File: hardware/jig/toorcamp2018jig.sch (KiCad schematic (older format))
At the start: 76 parts, among them J1 NEIGHBOR1, J2 NEIGHBOR2, J3 GOODFET, J4 TOP_INTERCONNECT, J5 BACK_INTERCONNECT, J6 FAULT, J7 BONUS_ROW, J8 TEST_2P, J9 TEST_2P, P1 CONN_01X02, P10 CONN_01X02, P11 CONN_01X02, P12 CONN_01X02, P13 CONN_01X02, P14 CONN_01X02, P2 CONN_01X02, P3 CONN_01X02, P4 CONN_01X02, P5 CONN_01X02, P6 CONN_01X02, P7 CONN_01X02, P8 CONN_01X02, P9 CONN_01X02, U1 NX5P2553GV

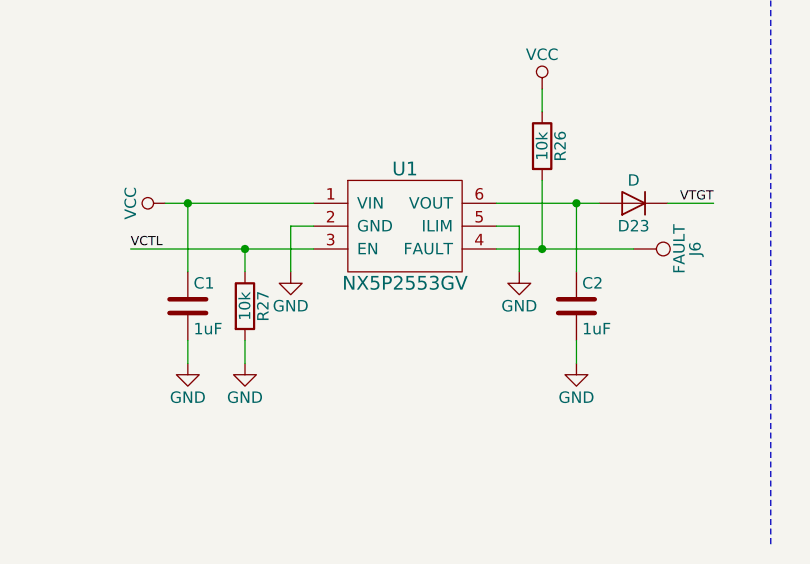
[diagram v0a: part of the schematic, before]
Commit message: filled in test jig bom info
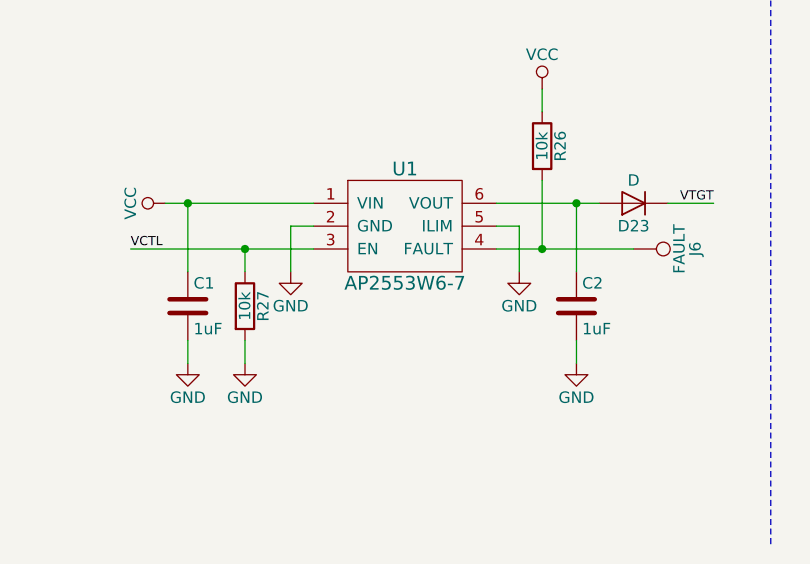
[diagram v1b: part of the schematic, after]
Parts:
- J1, J2: Description (none) -> CONN HEADER .100\" DUAL STR 40POS; Manufacturer (none) -> Sullins; Part Number (none) -> PRPC020DAAN-RC
- J4: Description (none) -> CONN RCPT .100\" 40POS DUAL-ROW GOLD; Manufacturer (none) -> Samtec; Part Number (none) -> SSW-120-01-F-D
- J5: Description (none) -> CONN HEADER .100\" DUAL R/A 40POS; Manufacturer (none) -> Sullins; Part Number (none) -> PRPC020DBAN-M71RC
- P1, P10, P11, P12, P13, P14, P2, P3, P4, P5, P6, P7, P8, P9: Description (none) -> CONN BATTERY 2 POS MINI; Manufacturer (none) -> AVX; Part Number (none) -> 009155002201006
- U1: value NX5P2553GV -> AP2553W6-7; Description (none) -> IC PD SW CURR LIMIT SOT26; Manufacturer (none) -> Diodes Inc.; Part Number (none) -> AP2553W6-7
